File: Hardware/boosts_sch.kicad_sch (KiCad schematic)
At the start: 45 parts, among them IC1 TPS61089RNRR, IC2 AP2205-W5-7, IC3 AP2205-W5-7, IC4 TPS61089RNRR

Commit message: wrapping up layout
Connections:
- net +3V3 renamed RBUS_uC_V

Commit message: layout
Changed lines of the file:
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@@
 	(wire
 		(pts
+			(xy 210.312 33.782) (xy 213.868 33.782)
+		)
+		(stroke
+			(width 0)
+			(type default)
+		)
+	)
+	(wire
+		(pts
 			(xy 39.37 110.49) (xy 39.37 110.744)
 		)
@@
 	(wire
 		(pts
+			(xy 104.902 37.592) (xy 108.712 37.592)
+		)
+		(stroke
+			(width 0)
+			(type default)
+		)
+	)
+	(wire
+		(pts
 			(xy 167.132 54.102) (xy 177.292 54.102)
 		)
@@
 		(lib_name "GND_1")
 		(lib_id "power:GND")
-		(at 104.902 37.592 180)
+		(at 108.712 37.592 0)
 		(unit 1)
 		(exclude_from_sim no)
@@
 		(dnp no)
 		(property "Reference" "#PWR060"
-			(at 104.902 31.242 0)
+			(at 108.712 43.942 0)
 			(effects
 				(font
@@
 		)
 		(property "Value" "GND"
-			(at 104.902 32.512 0)
+			(at 108.712 42.672 0)
 			(effects
 				(font
@@
 		)
 		(property "Footprint" ""
-			(at 104.902 37.592 0)
+			(at 108.712 37.592 0)
 			(effects
 				(font
@@
 		)
 		(property "Datasheet" ""
-			(at 104.902 37.592 0)
+			(at 108.712 37.592 0)
 			(effects
 				(font
@@
 		)
 		(property "Description" ""
-			(at 104.902 37.592 0)
+			(at 108.712 37.592 0)
 			(effects
 				(font
@@
 		(lib_name "GND_1")
 		(lib_id "power:GND")
-		(at 210.312 33.782 180)
+		(at 213.868 33.782 0)
 		(unit 1)
 		(exclude_from_sim no)
@@
 		(dnp no)
 		(property "Reference" "#PWR073"
-			(at 210.312 27.432 0)
+			(at 213.868 40.132 0)
 			(effects
 				(font
@@
 		)
 		(property "Value" "GND"
-			(at 210.312 28.702 0)
+			(at 213.868 38.862 0)
 			(effects
 				(font
@@
 		)
 		(property "Footprint" ""
-			(at 210.312 33.782 0)
+			(at 213.868 33.782 0)
 			(effects
 				(font
@@
 		)
 		(property "Datasheet" ""
-			(at 210.312 33.782 0)
+			(at 213.868 33.782 0)
 			(effects
 				(font
@@
 		)
 		(property "Description" ""
-			(at 210.312 33.782 0)
+			(at 213.868 33.782 0)
 			(effects
 				(font

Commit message: added diodes on gpio breakout and sensor supply
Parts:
- added D3: MMBZ6V2ALT1G, Package_TO_SOT_SMD:SOT-23, symbol Power_Protection:SP0502BAHT
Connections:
- net 5V: now also D3.1 (K)
- net GND: now also D3.3 (A)
- net RBUS_uC_V renamed +3V3
- no-connect marks 0 -> 1

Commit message: changed ldo output to 12v, kiran review done
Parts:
- added R65: 360k, Resistor_SMD:R_0402_1005Metric, symbol Device:R_Small
- R23: footprint Resistor_SMD:R_0603_1608Metric -> Resistor_SMD:R_0402_1005Metric
- R26: value 900k -> 976k
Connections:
- net 12V: now also R65.2
- net at IC3.4 (ADJ/NC), R28.2: now also R65.1
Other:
- note added: "973k"
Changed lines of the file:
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@@
 	)
 	(junction
-		(at 66.548 139.192)
+		(at 119.888 49.022)
 		(diameter 0)
 		(color 0 0 0 0)
 	)
 	(junction
-		(at 119.888 49.022)
+		(at 107.95 113.03)
 		(diameter 0)
 		(color 0 0 0 0)
 	)
 	(junction
-		(at 107.95 113.03)
+		(at 212.852 43.942)
 		(diameter 0)
 		(color 0 0 0 0)
 	)
 	(junction
-		(at 212.852 43.942)
+		(at 210.312 38.862)
 		(diameter 0)
 		(color 0 0 0 0)
@@
 	)
 	(junction
+		(at 210.312 43.942)
+		(diameter 0)
+		(color 0 0 0 0)
+	)
+	(junction
 		(at 61.722 46.482)
 		(diameter 0)
@@
 	)
 	(junction
+		(at 67.31 138.684)
+		(diameter 0)
+		(color 0 0 0 0)
+	)
+	(junction
 		(at 104.902 43.942)
 		(diameter 0)
@@
 	(wire
 		(pts
-			(xy 222.504 103.632) (xy 231.648 103.632)
+			(xy 67.31 137.16) (xy 67.31 138.684)
 		)
 		(stroke
@@
 	(wire
 		(pts
-			(xy 225.552 111.506) (xy 225.552 111.76)
+			(xy 222.504 103.632) (xy 231.648 103.632)
 		)
 		(stroke
@@
 	(wire
 		(pts
-			(xy 158.242 41.402) (xy 162.052 41.402)
+			(xy 225.552 111.506) (xy 225.552 111.76)
 		)
 		(stroke
@@
 	(wire
 		(pts
-			(xy 61.722 46.482) (xy 71.882 46.482)
+			(xy 158.242 41.402) (xy 162.052 41.402)
 		)
 		(stroke
@@
 	(wire
 		(pts
-			(xy 65.786 120.65) (xy 65.786 132.08)
+			(xy 61.722 46.482) (xy 71.882 46.482)
 		)
 		(stroke
@@
 	(wire
 		(pts
-			(xy 70.358 139.446) (xy 70.358 138.938)
+			(xy 65.786 120.65) (xy 65.786 132.08)
 		)
 		(stroke
@@
 	(wire
 		(pts
-			(xy 66.548 139.446) (xy 66.548 139.192)
-		)
-		(stroke
-			(width 0)
-			(type default)
-		)
-	)
-	(wire
-		(pts
 			(xy 102.362 43.942) (xy 102.362 46.482)
 		)
@@
 	(wire
 		(pts
-			(xy 222.504 94.488) (xy 222.504 98.552)
+			(xy 67.31 138.684) (xy 67.31 139.192)
 		)
 		(stroke
@@
 	(wire
 		(pts
-			(xy 225.552 106.172) (xy 225.552 106.426)
+			(xy 222.504 94.488) (xy 222.504 98.552)
 		)
 		(stroke
@@
 	(wire
 		(pts
-			(xy 207.772 38.862) (xy 207.772 41.402)
+			(xy 225.552 106.172) (xy 225.552 106.426)
 		)
 		(stroke
@@
 	(wire
 		(pts
-			(xy 93.726 113.03) (xy 102.87 113.03)
+			(xy 207.772 38.862) (xy 207.772 41.402)
 		)
 		(stroke
@@
 	(wire
 		(pts
-			(xy 207.772 43.942) (xy 212.852 43.942)
+			(xy 93.726 113.03) (xy 102.87 113.03)
 		)
 		(stroke
@@
 	(wire
 		(pts
-			(xy 66.548 137.16) (xy 67.31 137.16)
+			(xy 207.772 43.942) (xy 210.312 43.942)
 		)
 		(stroke
@@
 	(wire
 		(pts
-			(xy 66.548 137.16) (xy 66.548 139.192)
-		)
-		(stroke
-			(width 0)
-			(type default)
-		)
-	)
-	(wire
-		(pts
 			(xy 172.974 106.172) (xy 181.102 106.172)
 		)
@@
 	(wire
 		(pts
-			(xy 66.548 139.192) (xy 67.31 139.192)
-		)
-		(stroke
-			(width 0)
-			(type default)
-		)
-	)
-	(wire
-		(pts
 			(xy 110.744 133.35) (xy 114.554 133.35)
 		)
@@
 	(wire
 		(pts
+			(xy 67.31 138.684) (xy 69.596 138.684)
+		)
+		(stroke
+			(width 0)
+			(type default)
+		)
+	)
+	(wire
+		(pts
 			(xy 104.902 37.592) (xy 108.712 37.592)
 		)
@@
 	(wire
 		(pts
-			(xy 67.31 132.08) (xy 81.026 132.08)
+			(xy 210.312 43.942) (xy 212.852 43.942)
 		)
 		(stroke
@@
 	(wire
 		(pts
-			(xy 93.726 121.158) (xy 96.774 121.158)
+			(xy 67.31 132.08) (xy 81.026 132.08)
 		)
 		(stroke
@@
 	(wire
 		(pts
-			(xy 96.774 115.57) (xy 96.774 115.824)
+			(xy 93.726 121.158) (xy 96.774 121.158)
 		)
 		(stroke
@@
 	(wire
 		(pts
-			(xy 107.442 49.022) (xy 104.902 49.022)
+			(xy 96.774 115.57) (xy 96.774 115.824)
 		)
 		(stroke
@@
 	(wire
 		(pts
-			(xy 66.548 139.446) (xy 70.358 139.446)
+			(xy 107.442 49.022) (xy 104.902 49.022)
 		)
 		(stroke
@@
 		)
 	)
+	(text "973k\n"
+		(exclude_from_sim no)
+		(at 180.594 134.62 0)
+		(effects
+			(font
+				(size 1.27 1.27)
+			)
+		)
+	)
 	(text "SIM: https://webench.ti.com/appinfo/webench/scripts/SDP.cgi?ID=0086ECB0F8B2BBA7"
 		(exclude_from_sim no)
@@
 	)
 	(label "FB_5V"
-		(at 70.358 139.446 0)
+		(at 69.596 138.684 0)
 		(fields_autoplaced yes)
 		(effects
@@
 	)
 	(symbol
+		(lib_id "Device:R_Small")
+		(at 210.312 41.402 0)
+		(unit 1)
+		(exclude_from_sim no)
+		(in_bom yes)
+		(on_board yes)
+		(dnp no)
+		(fields_autoplaced yes)
+		(property "Reference" "R65"
+			(at 211.8106 40.1898 0)
+			(effects
+				(font
+					(size 1.27 1.27)
+				)
+				(justify left)
+			)
+		)
+		(property "Value" "360k"
+			(at 211.8106 42.6141 0)
+			(effects
+				(font
+					(size 1.27 1.27)
+				)
+				(justify left)
+			)
+		)
+		(property "Footprint" "Resistor_SMD:R_0402_1005Metric"
+			(at 210.312 41.402 0)
+			(effects
+				(font
+					(size 1.27 1.27)
+				)
+				(hide yes)
+			)
+		)
+		(property "Datasheet" "~"
+			(at 210.312 41.402 0)
+			(effects
+				(font
+					(size 1.27 1.27)
+				)
+				(hide yes)
+			)
+		)
+		(property "Description" ""
+			(at 210.312 41.402 0)
+			(effects
+				(font
+					(size 1.27 1.27)
+				)
+				(hide yes)
+			)
+		)
+		(pin "1"
+		)
+		(pin "2"
+		)
+		(instances
+			(project "Ricardo-Kermit-Mini"
+				(path "/7db990e4-92e1-4f99-b4d2-435bbec1ba83/4e53c9d6-58b6-437c-afe4-98fd8bd012ed"
+					(reference "R65")
+					(unit 1)
+				)
+			)
+		)
+	)
+	(symbol
 		(lib_id "Device:C_Small")
 		(at 87.884 134.62 0)
@@
 		(fields_autoplaced yes)
 		(property "Reference" "R26"
-			(at 198.12 123.952 0)
+			(at 197.5866 124.0098 0)
 			(effects
 				(font
@@
 			)
 		)
-		(property "Value" "900k"
-			(at 198.12 126.492 0)
+		(property "Value" "976k"
+			(at 197.5866 126.4341 0)
 			(effects
 				(font
@@
 			)
 		)
-		(property "Footprint" "Resistor_SMD:R_0603_1608Metric"
+		(property "Footprint" "Resistor_SMD:R_0402_1005Metric"
 			(at 104.902 46.482 0)
 			(effects
@@
 		)
 		(property "Value" "GND"
-			(at 213.868 38.862 0)
+			(at 217.424 35.56 0)
 			(effects
 				(font

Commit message: update
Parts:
- D3: MPN (none) -> MMBZ6V2ALT1G
- IC1, IC4: MPN (none) -> TPS61089RNRR
- IC2, IC3: MPN (none) -> AP2205-W5-7
- R23: value 152k -> 150k
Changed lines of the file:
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@@
 			)
 		)
+		(property "MPN" "TPS61089RNRR"
+			(at 194.564 98.552 0)
+			(effects
+				(font
+					(size 1.27 1.27)
+				)
+				(hide yes)
+			)
+		)
 		(pin "1"
 		)
@@
 			)
 		)
+		(property "MPN" "MMBZ6V2ALT1G"
+			(at 122.428 56.896 0)
+			(effects
+				(font
+					(size 1.27 1.27)
+				)
+				(hide yes)
+			)
+		)
 		(pin "2"
 		)
@@
 			)
 		)
+		(property "MPN" "AP2205-W5-7"
+			(at 177.292 41.402 0)
+			(effects
+				(font
+					(size 1.27 1.27)
+				)
+				(hide yes)
+			)
+		)
 		(pin "1"
 		)
@@
 			)
 		)
+		(property "MPN" "TPS61089RNRR"
+			(at 65.786 107.95 0)
+			(effects
+				(font
+					(size 1.27 1.27)
+				)
+				(hide yes)
+			)
+		)
 		(pin "1"
 		)
@@
 			)
 		)
+		(property "MPN" "AP2205-W5-7"
+			(at 71.882 46.482 0)
+			(effects
+				(font
+					(size 1.27 1.27)
+				)
+				(hide yes)
+			)
+		)
 		(pin "1"
 		)
@@
 			)
 		)
-		(property "Value" "152k"
+		(property "Value" "150k"
 			(at 107.442 48.387 0)
 			(effects

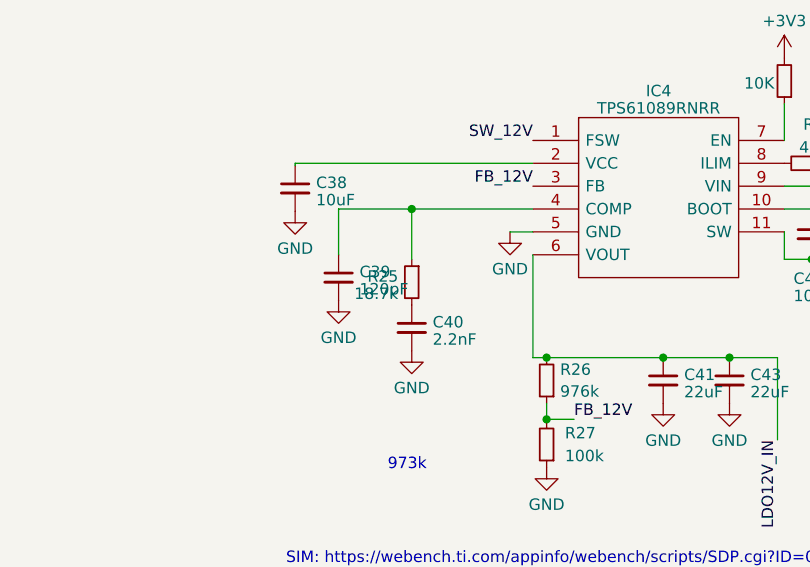
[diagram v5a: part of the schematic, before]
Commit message: changed boost output cap to 0603
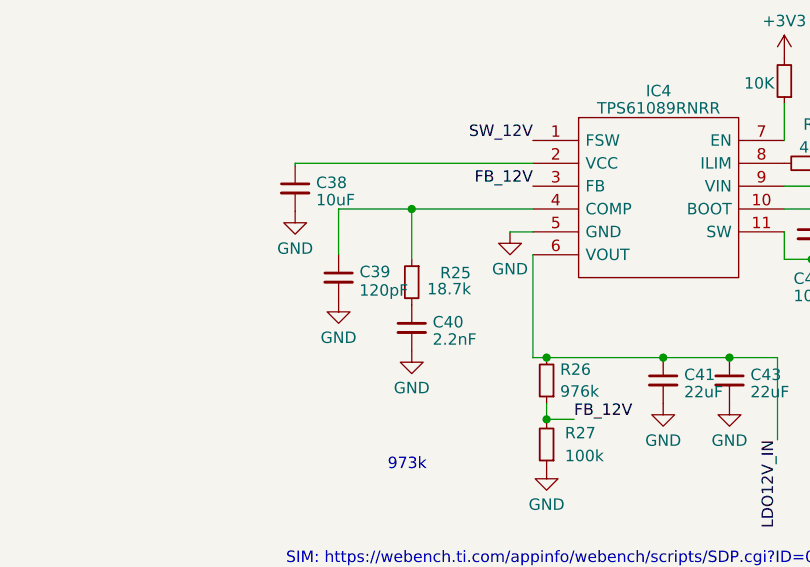
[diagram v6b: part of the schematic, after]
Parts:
- C28, C37: MPN (none) -> CL05X105KA5NQNC
- C32, C42: MPN (none) -> GRM155R61E225ME15D
- C35: MPN (none) -> TMK107BBJ106MA-T
- C36, C47: MPN (none) -> C1005X5R1E104KT000E
- C46: footprint Capacitor_SMD:C_0402_1005Metric -> Capacitor_SMD:C_0603_1608Metric; MPN (none) -> TMK107BBJ106MA-T
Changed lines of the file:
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@@
 			)
 		)
+		(property "MPN" "C1005X5R1E104KT000E"
+			(at 247.142 49.022 0)
+			(effects
+				(font
+					(size 1.27 1.27)
+				)
+				(hide yes)
+			)
+		)
 		(pin "1"
 		)
@@
 			)
 		)
-		(property "Footprint" "Capacitor_SMD:C_0402_1005Metric"
+		(property "Footprint" "Capacitor_SMD:C_0603_1608Metric"
 			(at 239.522 49.022 0)
 			(effects
@@
 			)
 		)
+		(property "MPN" " TMK107BBJ106MA-T"
+			(at 239.522 49.022 0)
+			(effects
+				(font
+					(size 1.27 1.27)
+				)
+				(hide yes)
+			)
+		)
 		(pin "1"
 		)
@@
 			)
 		)
+		(property "MPN" "GRM155R61E225ME15D"
+			(at 107.442 54.102 0)
+			(effects
+				(font
+					(size 1.27 1.27)
+				)
+				(hide yes)
+			)
+		)
 		(pin "1"
 		)
@@
 		(dnp no)
 		(property "Reference" "R25"
-			(at 179.6034 113.6563 0)
+			(at 187.6806 113.2767 0)
 			(effects
 				(font
@@
 		)
 		(property "Value" "18.7k"
-			(at 179.6034 115.5773 0)
+			(at 187.706 115.062 0)
 			(effects
 				(font
@@
 			)
 		)
+		(property "MPN" "CL05X105KA5NQNC"
+			(at 56.642 49.022 0)
+			(effects
+				(font
+					(size 1.27 1.27)
+				)
+				(hide yes)
+			)
+		)
 		(pin "1"
 		)
@@
 		(on_board yes)
 		(dnp no)
-		(fields_autoplaced yes)
 		(property "Reference" "C39"
 			(at 175.2981 113.1546 0)
@@
 		)
 		(property "Value" "120pF"
-			(at 175.2981 115.0756 0)
+			(at 175.2727 115.2113 0)
 			(effects
 				(font
@@
 			)
 		)
+		(property "MPN" " TMK107BBJ106MA-T"
+			(at 123.952 78.232 0)
+			(effects
+				(font
+					(size 1.27 1.27)
+				)
+				(hide yes)
+			)
+		)
 		(pin "1"
 		)
@@
 			)
 		)
+		(property "MPN" "CL05X105KA5NQNC"
+			(at 162.052 43.942 0)
+			(effects
+				(font
+					(size 1.27 1.27)
+				)
+				(hide yes)
+			)
+		)
 		(pin "1"
 		)
@@
 			)
 		)
+		(property "MPN" "C1005X5R1E104KT000E"
+			(at 131.572 78.232 0)
+			(effects
+				(font
+					(size 1.27 1.27)
+				)
+				(hide yes)
+			)
+		)
 		(pin "1"
 		)
@@
 			(at 212.852 49.022 0)
 			(effects
+				(font
+					(size 1.27 1.27)
+				)
+				(hide yes)
+			)
+		)
+		(property "MPN" "GRM155R61E225ME15D"
+			(at 212.852 49.022 0)
+			(effects

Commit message: update
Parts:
- C35: MPN TMK107BBJ106MA-T -> CL05A106MP8NUB8
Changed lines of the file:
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@@
 			)
 		)
-		(property "MPN" " TMK107BBJ106MA-T"
+		(property "MPN" " CL05A106MP8NUB8"
 			(at 123.952 78.232 0)
 			(effects

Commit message: changes post 3rd review
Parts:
- R22: value 50k -> 49.9k
- R28: value 51k -> 49.9
- R65: value 360k -> 432k
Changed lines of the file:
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@@
 		(on_board yes)
 		(dnp no)
-		(fields_autoplaced yes)
 		(property "Reference" "R22"
-			(at 102.362 40.767 0)
-			(effects
-				(font
-					(size 1.27 1.27)
-				)
-				(justify right)
-			)
-		)
-		(property "Value" "50k"
-			(at 102.362 38.227 0)
-			(effects
-				(font
-					(size 1.27 1.27)
-				)
-				(justify right)
+			(at 98.298 38.608 0)
+			(effects
+				(font
+					(size 1.27 1.27)
+				)
+				(justify left)
+			)
+		)
+		(property "Value" "49.9k"
+			(at 98.298 41.0323 0)
+			(effects
+				(font
+					(size 1.27 1.27)
+				)
+				(justify left)
 			)
 		)
@@
 			)
 		)
-		(property "Value" "360k"
+		(property "Value" "432k"
 			(at 211.8106 42.6141 0)
 			(effects
@@
 		(on_board yes)
 		(dnp no)
-		(fields_autoplaced yes)
 		(property "Reference" "R28"
-			(at 207.772 36.957 0)
-			(effects
-				(font
-					(size 1.27 1.27)
-				)
-				(justify right)
-			)
-		)
-		(property "Value" "51k"
-			(at 207.772 34.417 0)
-			(effects
-				(font
-					(size 1.27 1.27)
-				)
-				(justify right)
-			)
-		)
+			(at 204.216 34.798 0)
+			(effects
+				(font
+					(size 1.27 1.27)
+				)
+				(justify left)
+			)
+		)
+		(property "Value" "49.9"
+			(at 204.216 37.2223 0)
+			(effects
+				(font
+					(size 1.27 1.27)
+				)
+				(justify left)
+			)
+		)
